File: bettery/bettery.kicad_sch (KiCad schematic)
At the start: 71 parts, among them J2 Conn_01x10_Socket, J4 Conn_ARM_SWD_TagConnect_TC2030, Q1 WMB014N06LG4, Q2 WMB014N06LG4, U1 L9961, U2 STM32G070KBTx

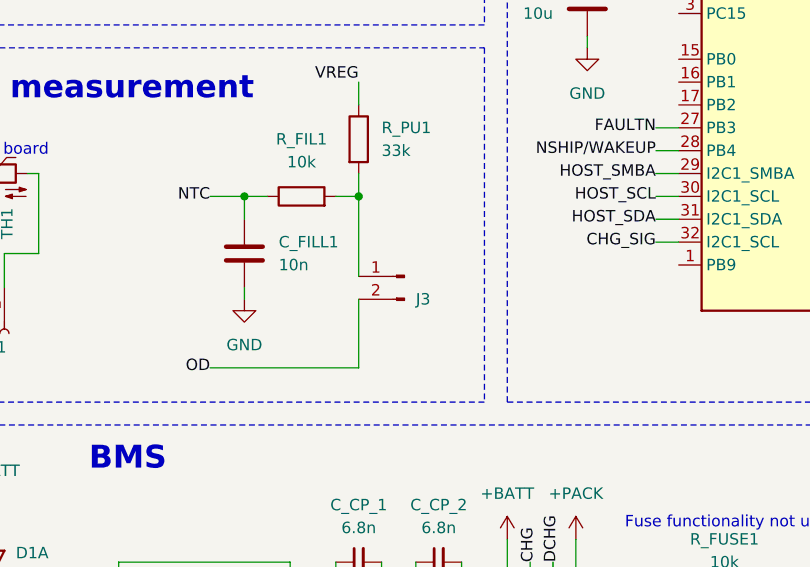
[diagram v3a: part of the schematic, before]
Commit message: move ntc connector to top side of the board
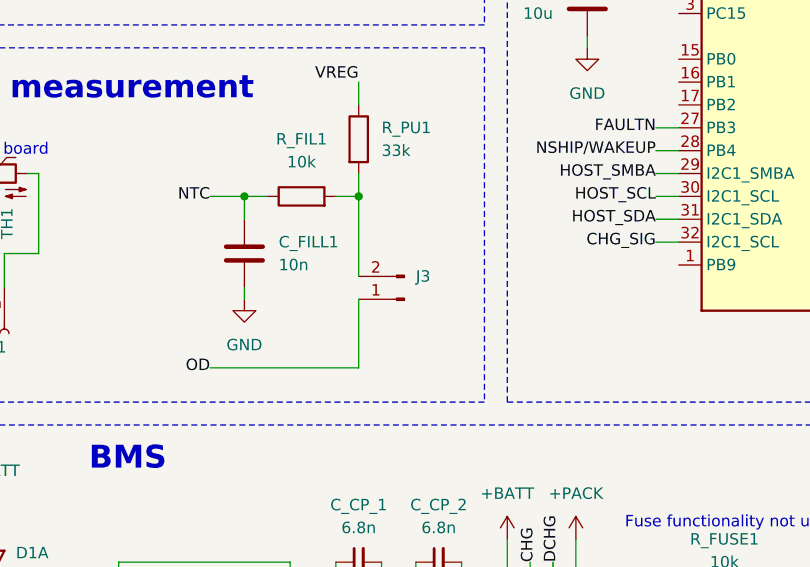
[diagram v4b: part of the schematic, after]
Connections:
- net OD: now also J3.1 (Pin_1); no longer J3.2 (Pin_2)
- net at R_FIL1.2, R_PU1.2: now also J3.2 (Pin_2); no longer J3.1 (Pin_1)
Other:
- moved on the sheet: J3
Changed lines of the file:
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@@
 	)
 	(junction
-		(at 115.57 101.6)
-		(diameter 0)
-		(color 0 0 0 0)
-	)
-	(junction
 		(at 33.02 127)
 		(diameter 0)
@@
 	)
 	(junction
+		(at 115.57 101.6)
+		(diameter 0)
+		(color 0 0 0 0)
+	)
+	(junction
 		(at 97.79 173.99)
 		(diameter 0)
@@
 	(wire
 		(pts
-			(xy 115.57 113.03) (xy 115.57 120.65)
-		)
-		(stroke
-			(width 0)
-			(type default)
-		)
-	)
-	(wire
-		(pts
 			(xy 31.75 53.34) (xy 31.75 55.88)
 		)
@@
 	(wire
 		(pts
+			(xy 115.57 101.6) (xy 115.57 110.49)
+		)
+		(stroke
+			(width 0)
+			(type default)
+		)
+	)
+	(wire
+		(pts
 			(xy 228.6 119.38) (xy 228.6 120.65)
 		)
@@
 	(wire
 		(pts
+			(xy 115.57 113.03) (xy 115.57 120.65)
+		)
+		(stroke
+			(width 0)
+			(type default)
+		)
+	)
+	(wire
+		(pts
 			(xy 232.41 52.07) (xy 232.41 50.8)
 		)
@@
 	(wire
 		(pts
-			(xy 115.57 101.6) (xy 115.57 110.49)
-		)
-		(stroke
-			(width 0)
-			(type default)
-		)
-	)
-	(wire
-		(pts
 			(xy 262.89 57.15) (xy 266.7 57.15)
 		)
@@
 	(symbol
 		(lib_id "Connector:Conn_01x02_Pin")
-		(at 120.65 110.49 0)
-		(mirror y)
+		(at 120.65 113.03 180)
 		(unit 1)
 		(exclude_from_sim no)
@@
 		(dnp no)
 		(property "Reference" "J3"
-			(at 121.92 113.0301 0)
+			(at 121.92 110.4899 0)
 			(effects
 				(font
@@
 		)
 		(property "Value" "~"
-			(at 121.92 110.4901 0)
+			(at 121.92 113.0299 0)
 			(effects
 				(font
@@
 		)
 		(property "Footprint" "Connector_JST:JST_PH_S2B-PH-K_1x02_P2.00mm_Horizontal"
-			(at 120.65 110.49 0)
+			(at 120.65 113.03 0)
 			(effects
 				(font
@@
 		)
 		(property "Datasheet" "~"
-			(at 120.65 110.49 0)
+			(at 120.65 113.03 0)
 			(effects
 				(font
@@
 		)
 		(property "Description" "Generic connector, single row, 01x02, script generated"
-			(at 120.65 110.49 0)
+			(at 120.65 113.03 0)
 			(effects
 				(font

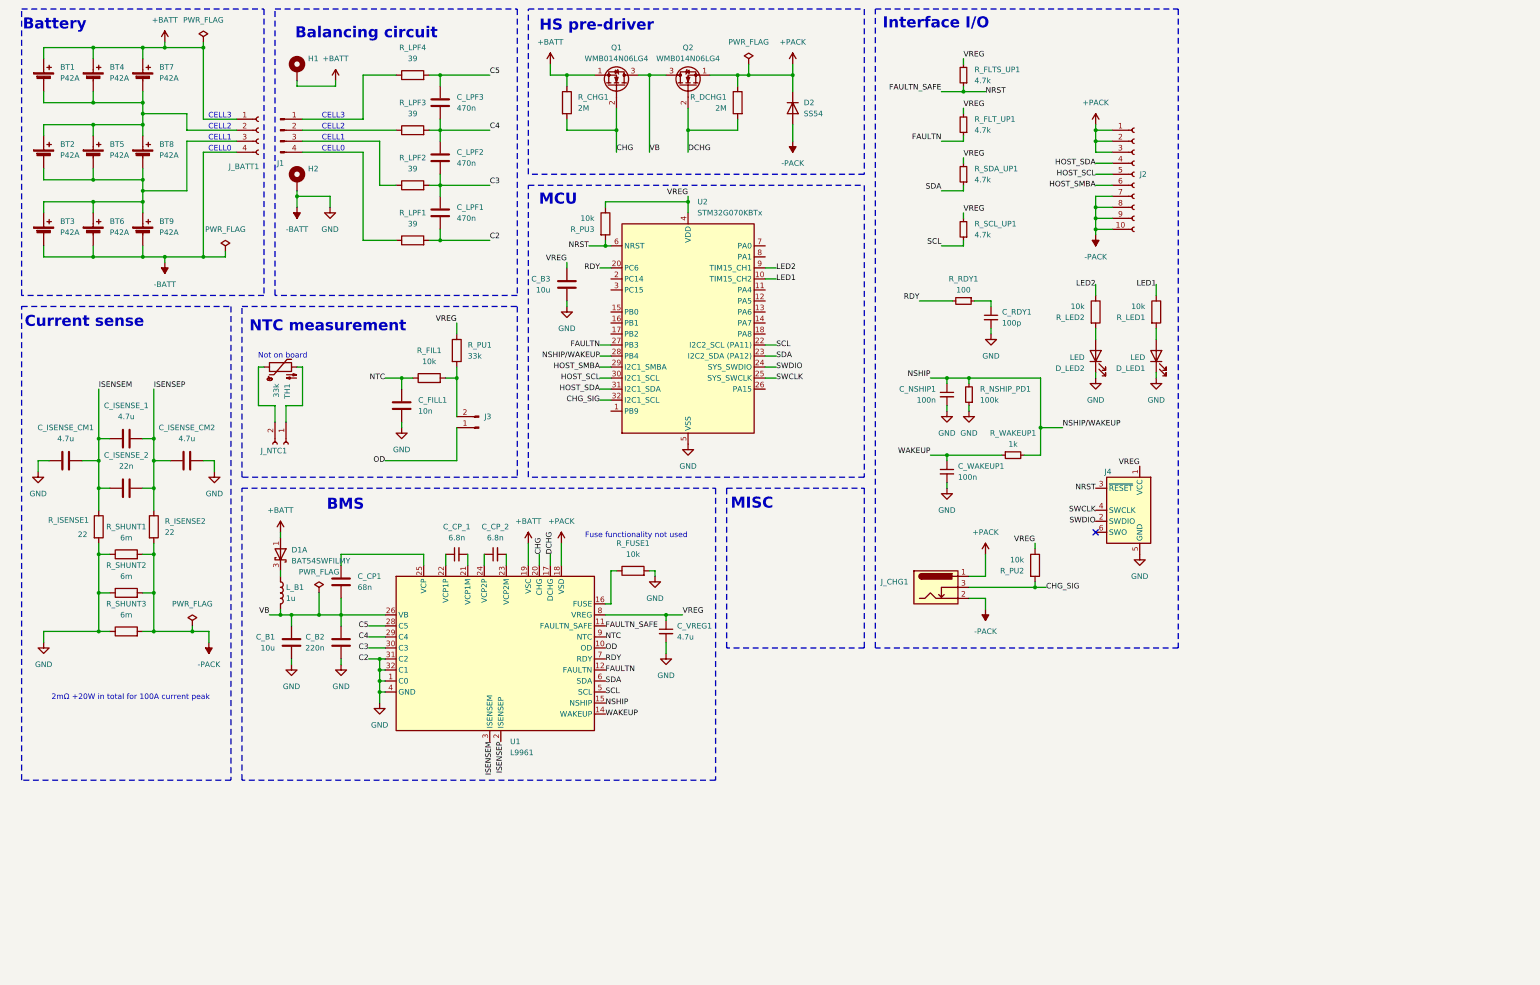
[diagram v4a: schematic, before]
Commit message: add chassis models
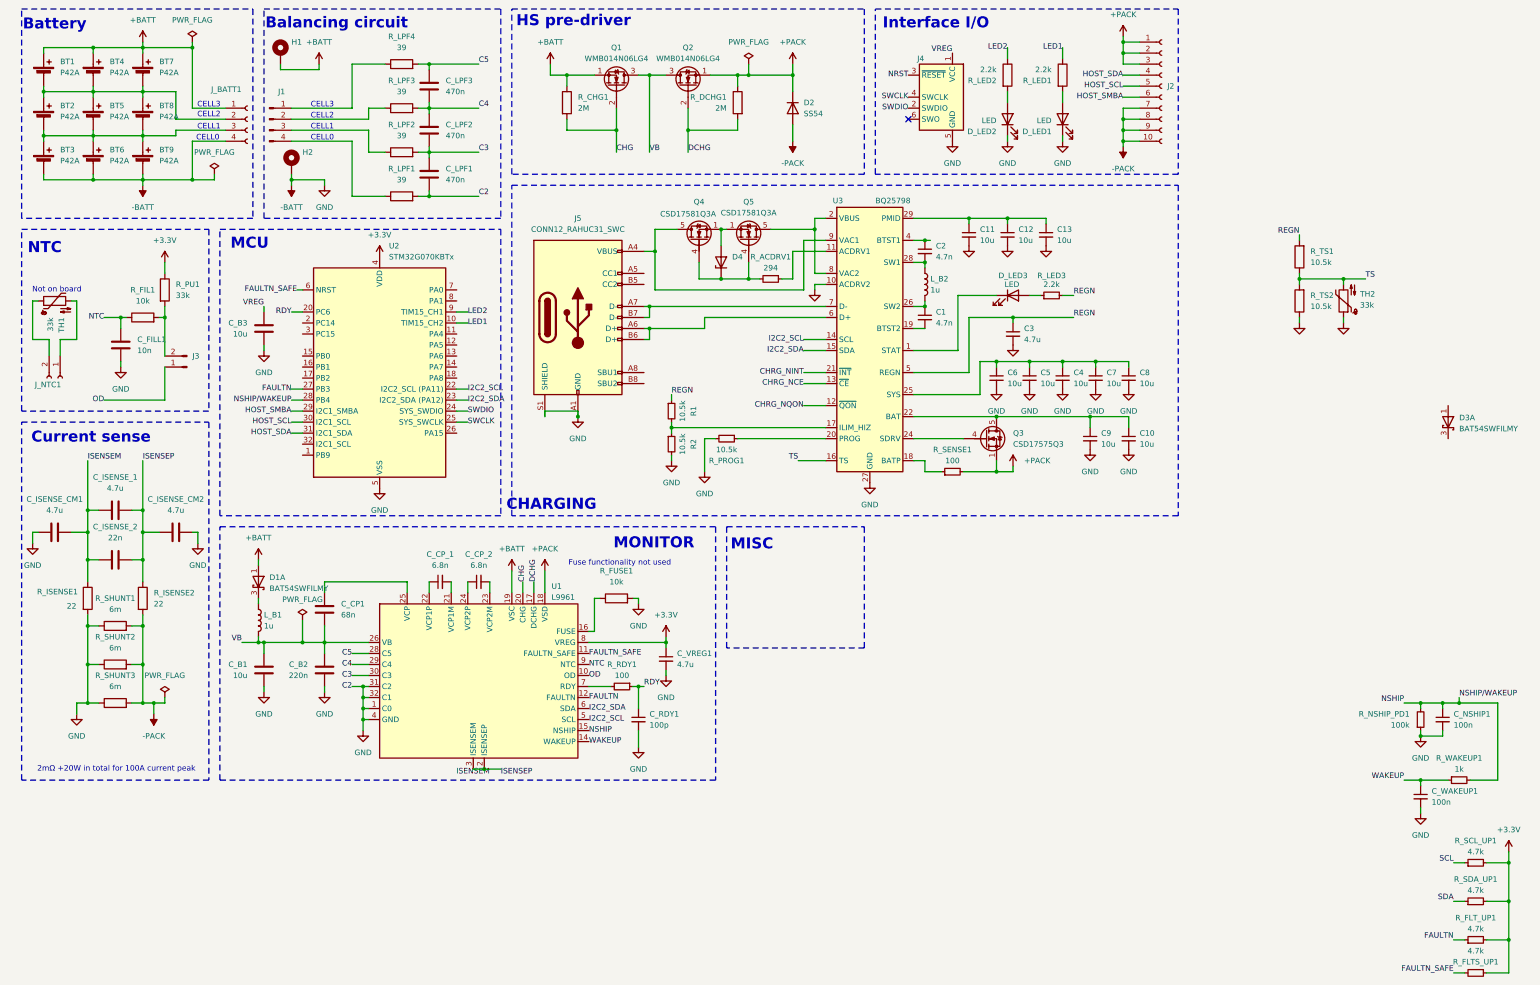
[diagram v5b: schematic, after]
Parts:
- removed J_CHG1: Barrel_Jack_Switch, Connector_BarrelJack:BarrelJack_GCT_DCJ200-10-A_Horizontal, symbol Connector:Barrel_Jack_Switch
- removed R_PU2, R_PU3: 10k, Resistor_SMD:R_0603_1608Metric, symbol Device:R
- added C1, C2: 4.7n, Capacitor_SMD:C_0603_1608Metric, symbol Device:C_Small
- added C10, C11, C12, C13, C4, C5, C6, C7, C8, C9: 10u, Capacitor_SMD:C_0603_1608Metric, symbol Device:C_Small
- added C3: 4.7u, Capacitor_SMD:C_0603_1608Metric, symbol Device:C_Small
- added D3: BAT54SWFILMY, Package_TO_SOT_SMD:SOT-323_SC-70, symbol Device:D_Schottky_Dual_CommonCathode_AAK_Split
- added D4: BZT52C12T-7, Diode_SMD:D_SOD-523, symbol Device:D_Zener
- added D_LED3: LED, LED_SMD:LED_0603_1608Metric, symbol Device:LED
- added J5: CONN12_RAHUC31_SWC, bettery:CONN12_RAHUC31_SWC, symbol bettery:CONN12_RAHUC31_SWC
- added L_B2: 1u, Inductor_SMD:L_Sumida_CDMC6D28_7.25x6.5mm, symbol Device:L
- added Q3: CSD17575Q3, Package_SON:VSON-8_3.3x3.3mm_P0.65mm_NexFET, symbol bettery:CSD17575Q3
- added Q4, Q5: CSD17581Q3A, Package_SON:VSON-8_3.3x3.3mm_P0.65mm_NexFET, symbol Transistor_FET:CSD17581Q3A
- added R1, R2, R_PROG1: 10.5k, Resistor_SMD:R_0603_1608Metric, symbol Device:R_Small
- added R_ACDRV1: 294, Resistor_SMD:R_0603_1608Metric, symbol Device:R_Small
- added R_LED3: 2.2k, Resistor_SMD:R_0603_1608Metric, symbol Device:R_Small
- added R_SENSE1: 100, Resistor_SMD:R_0603_1608Metric, symbol Device:R_Small
- added R_TS1, R_TS2: 10.5k, Resistor_SMD:R_0603_1608Metric, symbol Device:R
- added TH2: 33k, symbol Device:Thermistor_NTC
- added U3: BQ25798, Package_DFN_QFN:Texas_RQM0029A_VQFN-29_4x4mm_P0.4mm, symbol Battery_Management:BQ25798
- R_LED1, R_LED2: value 10k -> 2.2k
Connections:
- net ISENSEP is gone; now on net ISENSEM: C_ISENSE_1.2, C_ISENSE_2.2, C_ISENSE_CM2.1, R_ISENSE2.1, U1.2 (ISENSEP)
- net +PACK: now also Q3.1 (S), Q3.2 (S), Q3.3 (S), R_SENSE1.2
- net -BATT: now also C10.2, C11.2, C12.2, C13.2, C3.2, C4.2, C5.2, C6.2, C7.2, C8.2, C9.2, J5.A1 (GND), J5.B1 (GND), J5.S1 (SHIELD), R2.2, R_PROG1.2, R_TS2.1, TH2.1, U3.10 (ACDRV2), U3.27 (GND)
- net FAULTN_SAFE: now also R_FLTS_UP1.2; no longer J4.3 (~{RESET}), R_FLTS_UP1.1
- net RDY: now also C_RDY1.1, R_RDY1.1; no longer R_RDY1.2, U1.7 (RDY)
- net SCL: no longer U1.5 (SCL), U2.22 (PA9/PA11)
- net SDA: no longer U1.6 (SDA), U2.23 (PA10/PA12)
- net VREG: no longer C_VREG1.1, R_FLTS_UP1.2, R_FLT_UP1.2, R_PU1.1, R_SCL_UP1.2, R_SDA_UP1.2, U1.8 (VREG), U2.4 (VDD)
- net CHG_SIG: no longer names the net of U2.32 (PB8)
- new net: C10.1, C9.1, Q3.5 (D), U3.22 (BAT), U3.23 (BAT)
- new net: C2.2, L_B2.1, U3.28 (SW1)
- new net: C1.1, L_B2.2, U3.26 (SW2)
- new net: D_LED3.2 (A), R_LED3.1
- new net: C1.2, U3.19 (BTST2)
- new net: R_ACDRV1.1, U3.11 (ACDRV1)
- new net: D4.1 (K), Q4.4 (G), Q5.4 (G), R_ACDRV1.2
- new net: R_SENSE1.1, U3.18 (BATP)
- new net: C11.1, C12.1, C13.1, U3.29 (PMID)
- new net: D4.2 (A), Q4.1 (S), Q4.2 (S), Q4.3 (S), Q5.1 (S), Q5.2 (S), Q5.3 (S)
- new net: J5.A4 (VBUS), J5.B4 (VBUS), Q4.5 (D), U3.9 (VAC1)
- new net: Q3.4 (G), U3.24 (SDRV)
- new net: Q5.5 (D), U3.2 (VBUS), U3.3 (VBUS), U3.8 (VAC2)
- new net: R1.2, R2.1, U3.17 (ILIM_HIZ)
- new net: R_RDY1.2, U1.7 (RDY)
- new net: R_PROG1.1, U3.20 (PROG)
- new net: J5.A6 (D+), J5.B6 (D+), U3.6 (D+)
- new net: J5.A7 (D-), J5.B7 (D-), U3.7 (D-)
- new net: C4.1, C5.1, C6.1, C7.1, C8.1, U3.25 (SYS)
- new net: D_LED3.1 (K), U3.1 (STAT)
- new net: C2.1, U3.4 (BTST1)
- new net +3.3V: C_VREG1.1, R_FLTS_UP1.1, R_FLT_UP1.2, R_PU1.1, R_SCL_UP1.2, R_SDA_UP1.2, U1.8 (VREG), U2.4 (VDD)
- new net CHRG_NCE: U3.13 (~{CE})
- new net CHRG_NINT: U3.21 (~{INT})
- new net CHRG_NQON: U3.12 (~{QON})
- new net I2C2_SCL: U1.5 (SCL), U2.22 (PA9/PA11), U3.14 (SCL)
- new net I2C2_SDA: U1.6 (SDA), U2.23 (PA10/PA12), U3.15 (SDA)
- new net NRST: J4.3 (~{RESET})
- new net REGN: C3.1, R1.1, R_LED3.2, R_TS1.2, U3.5 (REGN)
- new net TS: R_TS1.1, R_TS2.2, TH2.2, U3.16 (TS)
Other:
- note added: "CHARGING"
- note added: "MONITOR"
- note added: "NTC"
- note removed: "BMS"
- note removed: "NTC measurement"
- moved on the sheet: BT1, BT2, BT3, BT4, BT5, BT6, BT7, BT8, BT9, C_B1, C_B2, C_B3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

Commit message: sync
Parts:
- J1, J3, J_NTC1: value ~ -> (none)
